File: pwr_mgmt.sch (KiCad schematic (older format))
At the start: 13 parts

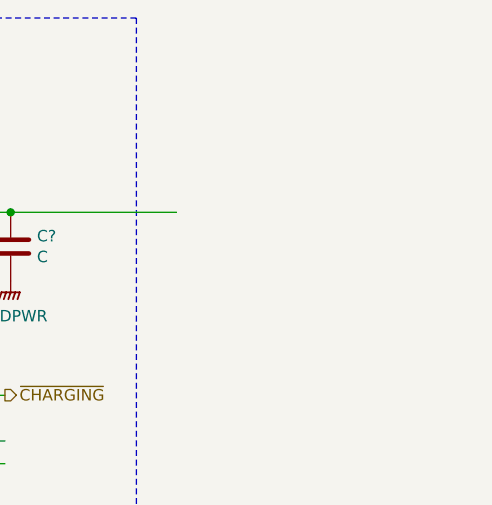
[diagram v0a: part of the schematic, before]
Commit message: Reshuffled MCU connections.
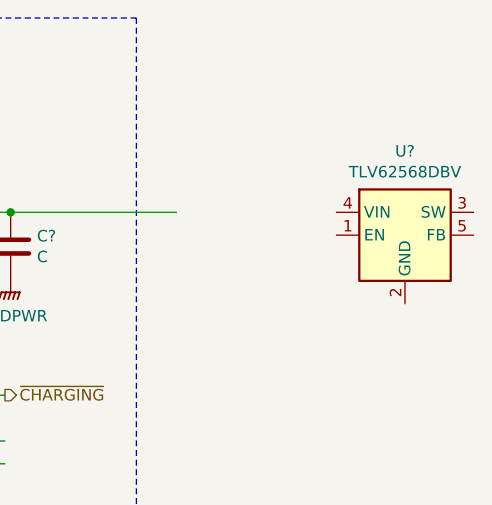
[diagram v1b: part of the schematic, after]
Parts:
- added U?: TLV62568DBV, Package_TO_SOT_SMD:SOT-23-5, symbol Regulator_Switching:TLV62568DBV
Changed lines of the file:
@@
 encoding utf-8
 Sheet 2 6
-Title ""
-Date ""
-Rev ""
-Comp ""
-Comment1 ""
-Comment2 ""
+Title "Rhea - Power Management Module"
+Date "2020-01-25"
+Rev "0.9.0"
+Comp "BME-VIK"
+Comment1 "Department of Measurement and Information Systems"
+Comment2 "Budapest University of Technology and Economics"
 Comment3 ""
-Comment4 ""
+Comment4 "Designed by: Peter Gyulai (BSc)"
 $EndDescr
 $Comp
@@
 I2C
 $Comp
-L power:GNDPWR #PWR?
+L power:GNDPWR #PWR0113
 U 1 1 5E37A880
 P 5325 2950
-F 0 "#PWR?" H 5325 2750 50  0001 C CNN
+F 0 "#PWR0113" H 5325 2750 50  0001 C CNN
 F 1 "GNDPWR" H 5329 2796 50  0000 C CNN
 F 2 "" H 5325 2900 50  0001 C CNN
@@
 $EndComp
 $Comp
-L power:GNDPWR #PWR?
+L power:GNDPWR #PWR0114
 U 1 1 5E37DC93
 P 3550 1450
-F 0 "#PWR?" H 3550 1250 50  0001 C CNN
+F 0 "#PWR0114" H 3550 1250 50  0001 C CNN
 F 1 "GNDPWR" H 3554 1296 50  0000 C CNN
 F 2 "" H 3550 1400 50  0001 C CNN
@@
 $EndComp
 $Comp
-L power:GNDPWR #PWR?
+L power:GNDPWR #PWR0115
 U 1 1 5E37FB01
 P 6350 2950
-F 0 "#PWR?" H 6350 2750 50  0001 C CNN
+F 0 "#PWR0115" H 6350 2750 50  0001 C CNN
 F 1 "GNDPWR" H 6354 2796 50  0000 C CNN
 F 2 "" H 6350 2900 50  0001 C CNN
@@
 Connection ~ 4425 1450
 $Comp
-L power:GNDD #PWR?
+L power:GNDD #PWR0116
 U 1 1 5E382DE3
 P 4550 2950
-F 0 "#PWR?" H 4550 2700 50  0001 C CNN
+F 0 "#PWR0116" H 4550 2700 50  0001 C CNN
 F 1 "GNDD" H 4554 2795 50  0000 C CNN
 F 2 "" H 4550 2950 50  0001 C CNN
@@
 	4200 2250 4625 2250
 $Comp
-L power:GNDA #PWR?
+L power:GNDA #PWR0117
 U 1 1 5E38609A
 P 3550 2925
-F 0 "#PWR?" H 3550 2675 50  0001 C CNN
+F 0 "#PWR0117" H 3550 2675 50  0001 C CNN
 F 1 "GNDA" H 3555 2752 50  0000 C CNN
 F 2 "" H 3550 2925 50  0001 C CNN
@@
 	4200 2550 4200 2925
 $Comp
-L power:GNDPWR #PWR?
+L power:GNDPWR #PWR0118
 U 1 1 5E386F12
 P 7600 1750
-F 0 "#PWR?" H 7600 1550 50  0001 C CNN
+F 0 "#PWR0118" H 7600 1550 50  0001 C CNN
 F 1 "GNDPWR" H 7604 1596 50  0000 C CNN
 F 2 "" H 7600 1700 50  0001 C CNN
@@
 	2575 1150 3550 1150
 Connection ~ 3550 1150
+$Comp
+L Regulator_Switching:TLV62568DBV U?
+U 1 1 5E379EA0
+P 9325 1550
+F 0 "U?" H 9325 1917 50  0000 C CNN
+F 1 "TLV62568DBV" H 9325 1826 50  0000 C CNN
+F 2 "Package_TO_SOT_SMD:SOT-23-5" H 9375 1300 50  0001 L CIN
+F 3 "http://www.ti.com/lit/ds/symlink/tlv62568.pdf" H 9075 2000 50  0001 C CNN
+	1    9325 1550
+	1    0    0    -1
+$EndComp
 $EndSCHEMATC

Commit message: Power management updates.
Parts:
- removed D?: D_Zener, symbol Device:D_Zener_ALT
- removed F?: Polyfuse, symbol Device:Polyfuse
- added C? (x3): C, symbol Device:C
- added F?: Polyfuse, symbol Device:Polyfuse
- added L?: L, symbol Device:L
- added R? (x2): R_US, symbol Device:R_US
- added U?: LF33_TO252, Package_TO_SOT_SMD:TO-252-2, symbol Regulator_Linear:LF33_TO252
- added U?: USB6B1, Package_SO:SOIC-8_3.9x4.9mm_P1.27mm, symbol Power_Protection:USB6B1
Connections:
- net labels added: 3V3_EXT, 3V3_REG, 3V3_SYS, I2C_SCL, I2C_SDA, USB_DATA+, USB_DATA-, USB_DATAN_IN, USB_DATAP_IN, ~BAT_LOW
- net labels removed: Earth
- wire segments 49 -> 76
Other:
- note added: "DC/DC Buck Regulator + LDO"
- note added: "PAC1720"
- note added: "PAC1932?"
- note added: "Power monitoring"
- note added: "USB Protection"
- note removed: "USB Connection"
- moved on the sheet: BT?, C?, D?, R?, TH?, U?

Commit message: Power management redesign started, and design documentation.
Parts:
- removed BT?: Li-Ion, symbol Device:Battery_Cell
- removed C? (x2): C, symbol Device:C
- removed R? (x5): R_US, symbol Device:R_US
- removed TH?: 10k, symbol Device:Thermistor_NTC
- removed U?: MCP73871, Package_DFN_QFN:QFN-20-1EP_4x4mm_P0.5mm_EP2.5x2.5mm, symbol Battery_Management:MCP73871
- added BT?: Li-Ion, symbol Device:Battery_Cell
- added C? (x2): C, symbol Device:C
- added R? (x8): R_US, symbol Device:R_US
- added TH?: 10k, symbol Device:Thermistor_NTC
- added U?: PAC1720, Package_DFN_QFN:DFN-10-1EP_3x3mm_P0.5mm_EP1.65x2.38mm, symbol Power_Supervisor:PAC1720
- added U?: STM6315, Package_TO_SOT_SMD:SOT-143, symbol Power_Supervisor:STM6315
- added U?: BQ24075, symbol Battery_Management:BQ24075
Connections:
- net labels added: RESET_IN, ~CONNECTED, ~POWER_ALERT, ~RESET
- net labels removed: POWER_ON, ~BAT_LOW
- wire segments 76 -> 89
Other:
- note added: "Li-Ion Battery Cell"
- note added: "Power-on reset"
- note removed: "PAC1720"
- note removed: "PAC1932?"
- moved on the sheet: C?, D?, F?, L?, R?, U?

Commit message: Power management & Documentation updates, source includes
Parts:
- removed BT?: Li-Ion, symbol Device:Battery_Cell
- removed C? (x2): C, symbol Device:C
- removed D?: D_Schottky, symbol Device:D_Schottky_ALT
- removed L?: L, symbol Device:L
- removed R? (x2): R_US, symbol Device:R_US
- removed U?: TLV62568DBV, Package_TO_SOT_SMD:SOT-23-5, symbol Regulator_Switching:TLV62568DBV
- removed U?: LF33_TO252, Package_TO_SOT_SMD:TO-252-2, symbol Regulator_Linear:LF33_TO252
- added BT?: Li-Ion, symbol Device:Battery_Cell
- added C? (x4): C, symbol Device:C
- added D?: D_Schottky, symbol Device:D_Schottky_ALT
- added L?: L, symbol Device:L
- added Q? (x2): Q_NMOS_DGS, symbol Device:Q_NMOS_DGS
- added R? (x4): R_US, symbol Device:R_US
- added U?: BQ297xy, Package_SON:WSON-6_1.5x1.5mm_P0.5mm, symbol Battery_Management:BQ297xy
- added U?: NCP186, symbol Regulator_Linear:NCP186
- added U?: NCP1529A, Package_TO_SOT_SMD:SOT-23-5, symbol Regulator_Switching:NCP1529A
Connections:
- net 3V3_REG: now also U?.1 (OUT), U?.2 (OUT), U?.4 (FB)
- net GNDA: now also R?.2
- net GNDPWR: now also C?.2, C?.2, Q?.3 (S), R?.2, U?.2 (GND), U?.5 (GND)
- net USB_5V: now also D?.2 (A)
- net at F?.2: now also D?.1 (K)
- net VIN_UNREG: now reaches C?.1, R?.1, R?.1, U?.10 (OUT), U?.11 (OUT)
- net VIN_UNREG: now also C?.1, U?.1 (EN), U?.4 (VIN)
- net PACK+: now reaches U?.2 (BAT), U?.3 (BAT)
- net PACK+: now also BT?.1 (+), R?.1
- new net: Q?.2 (G), U?.2 (Cout)
- new net: Q?.2 (G), U?.3 (Dout)
- new net: BT?.2 (-), C?.2, Q?.3 (S), U?.4 (VSS)
- new net: C?.1, R?.2, U?.5 (BAT)
- new net: R?.1, U?.6 (V-)
- new net: Q?.1 (D), Q?.1 (D)
- new net: C?.1, C?.1, L?.2, R?.1, U?.6 (EN), U?.7 (IN), U?.8 (IN)
- new net: L?.1, U?.3 (SW)
- new net: C?.2, R?.1, R?.2, U?.5 (FB)
- no-connect marks 0 -> 1
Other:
- note added: "Application notes:"
- note added: "Li-ion Battery Protection"
- moved on the sheet: C?, F?, R?, TH?, U?

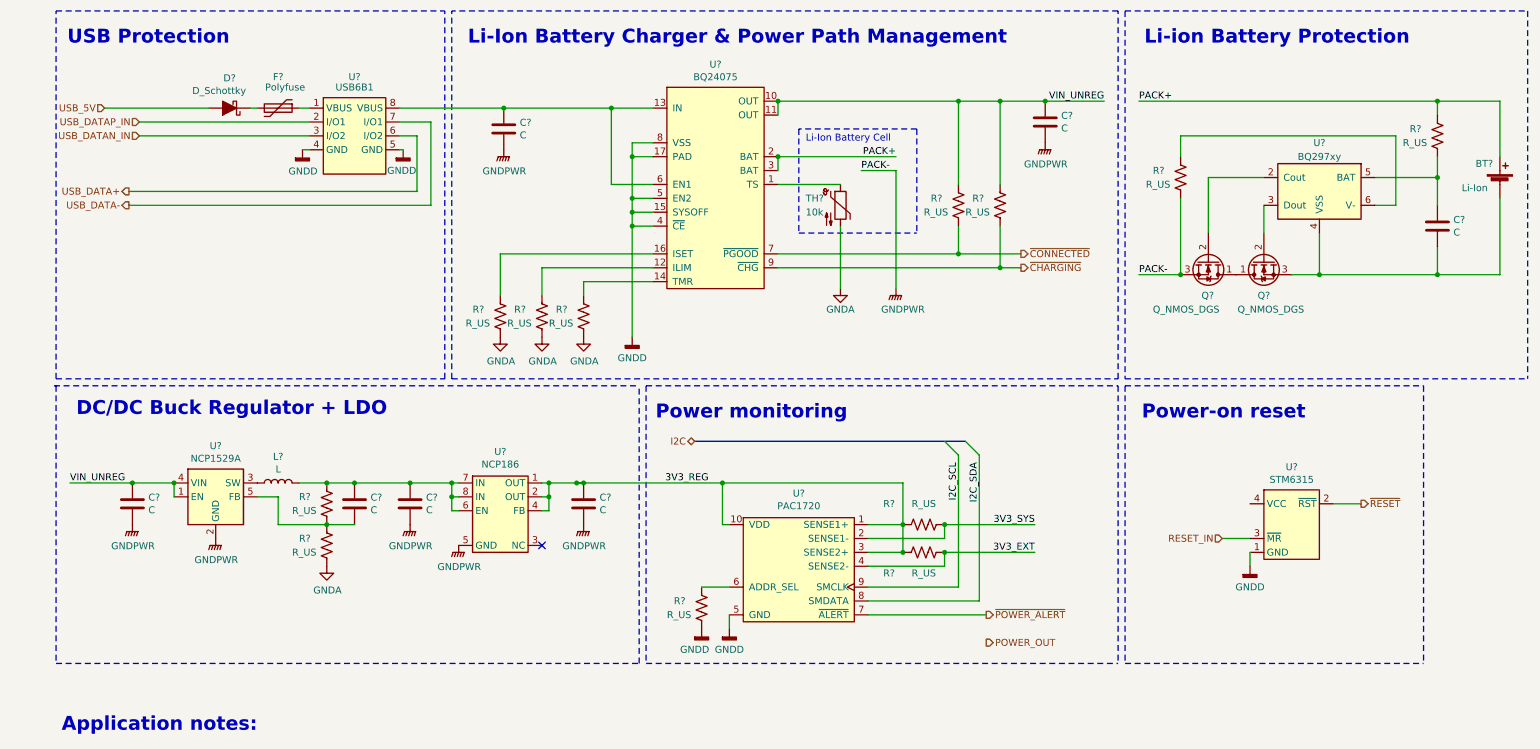
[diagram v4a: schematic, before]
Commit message: Automatic charge source selection & Documentation updates.
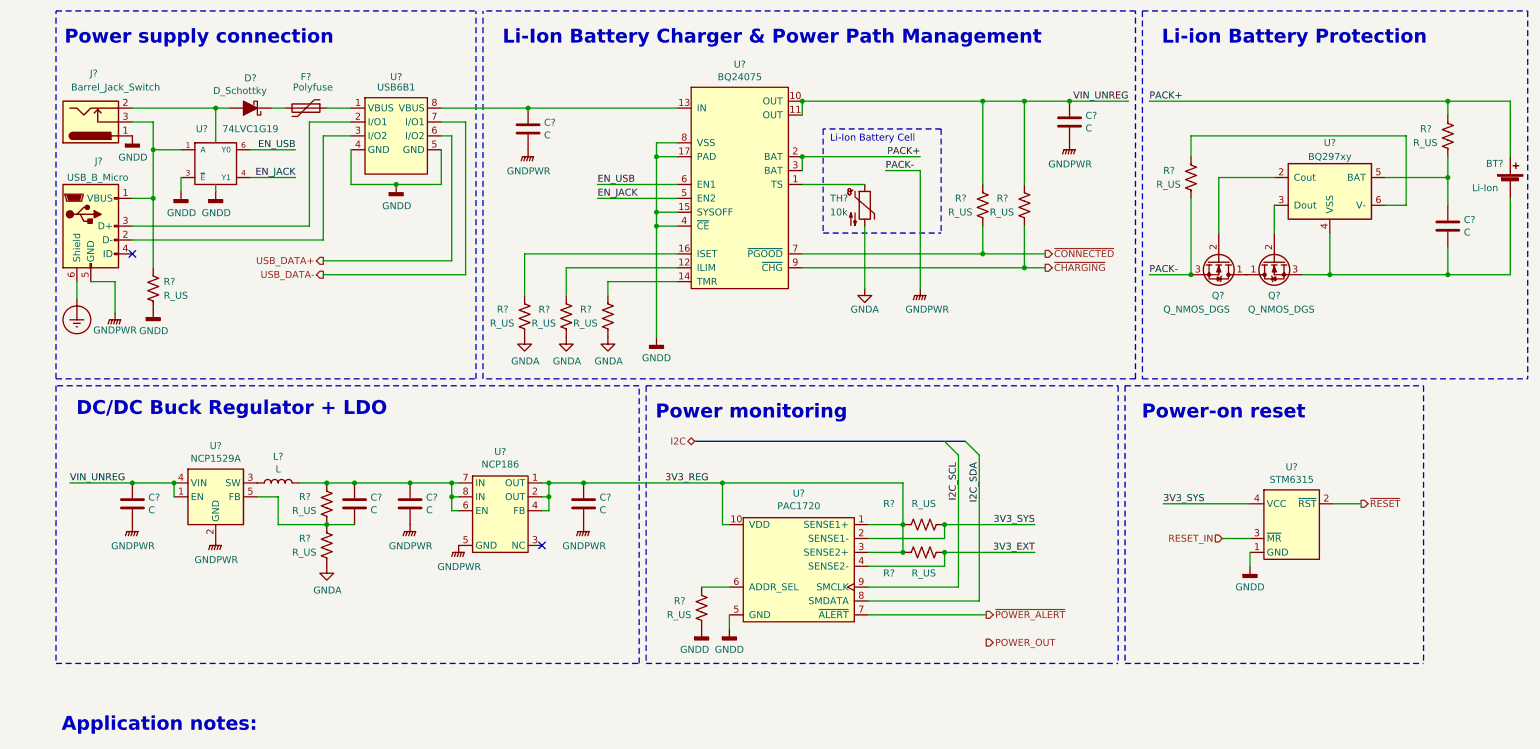
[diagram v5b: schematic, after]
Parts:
- added J?: Barrel_Jack_Switch, symbol Connector:Barrel_Jack_Switch
- added J?: USB_B_Micro, symbol Connector:USB_B_Micro
- added R?: R_US, symbol Device:R_US
- added U?: 74LVC1G19, symbol 74xGxx:74LVC1G19
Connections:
- net 3V3_SYS: now also U?.4 (VCC)
- net GNDPWR: now also J?.5 (GND)
- net at C?.1, U?.13 (IN), U?.8 (VBUS): no longer U?.6 (EN1)
- net GNDD renamed GND
- net GND: now also J?.1, R?.2, U?.2 (GND), U?.3 (~E); no longer U?.5 (EN2)
- net USB_5V renamed VCC
- net VCC: now also J?.2, U?.5 (VCC)
- net USB_DATAN_IN: no longer names the net of U?.3 (I/O2)
- net USB_DATAN_IN: now also J?.2 (D-)
- net USB_DATAP_IN: no longer names the net of U?.2 (I/O1)
- net USB_DATAP_IN: now also J?.3 (D+)
- new net: J?.1 (VBUS), J?.3, R?.1, U?.1 (A)
- new net EN_JACK: U?.4 (Y1), U?.5 (EN2)
- new net EN_USB: U?.6 (EN1), U?.6 (Y0)
- new net Earth_Protective: J?.6 (Shield)
- no-connect marks 1 -> 2
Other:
- note added: "Power supply connection"
- note removed: "USB Protection"
- moved on the sheet: BT?, C?, D?, F?, Q?, R?, TH?, U?

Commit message: Power regulation updates.
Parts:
- removed C?: C, symbol Device:C
- removed U?: NCP186, symbol Regulator_Linear:NCP186
- removed U?: NCP1529A, Package_TO_SOT_SMD:SOT-23-5, symbol Regulator_Switching:NCP1529A
- added C6: 10n, symbol Device:C
- added C?: 4.7u, symbol Device:C
- added D4: LED_CON, symbol Device:LED_ALT
- added D5: LED_CHG, symbol Device:LED_ALT
- added R10: 475k, symbol Device:R_US
- added U8: TLV62568DDC, Package_TO_SOT_SMD:SOT-23-6, symbol rhea_symbols:TLV62568DDC
- added U9: TPS73733DCQ, Package_TO_SOT_SMD:SOT-223-6, symbol Regulator_Linear:TPS73733DCQ
- C1, C2, C4: renamed from C?; value C -> 4.7u
- C3: renamed from C?; value C -> 0.1u
- C5, C7: renamed from C?; value C -> 10u
- L1: renamed from L?; value L -> 2.2u
- R1, R2: renamed from R?; value R_US -> 1.5k
- R13: renamed from R?; value R_US -> 100k
- R3: renamed from R?; value R_US -> 330R
- R5, R9: renamed from R?; value R_US -> 475k
- R6: renamed from R?; value R_US -> 510R
- R7: renamed from R?; value R_US -> 1k
- R8: renamed from R?; value R_US -> 50k
- U7: renamed from U?; value BQ297xy -> BQ29700
- gave numbers to parts that had none: 17
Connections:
- net 3V3_REG: now also U9.2 (OUT)
- net GNDA: now also C6.2
- net GNDPWR: now also C?.2, U8.2 (GND), U9.3 (GND)
- net PACK+: now also C?.1
- net VIN_UNREG: now also U8.1 (EN), U8.4 (VIN)
- net 3V45_REG: now reaches C5.1, L1.2, R9.1
- net 3V45_REG: now also R10.1, U9.1 (IN)
- net at L1.1: now also U8.3 (SW)
- net at R13.1, R9.2: now also U8.6 (FB)
- net ~CHARGING: no longer names the net of U6.9 (~CHG)
- net ~CHARGING: now also D5.1 (K); no longer R2.2
- net ~CONNECTED: no longer names the net of U6.7 (~PGOOD)
- net ~CONNECTED: now also D4.1 (K); no longer R1.2
- new net: D4.2 (A), R1.2
- new net: D5.2 (A), R2.2
- new net: C6.1, U9.4 (NR)
- new net: R10.2, U8.5 (PG), U9.5 (EN)
- no-connect marks 2 -> 1
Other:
- moved on the sheet: C3, C5, C7, Q1, Q2, R1, R13, R2, R3, U7
